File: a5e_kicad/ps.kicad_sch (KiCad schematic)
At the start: 52 parts, among them U1302 SIC931BED-T1-GE3

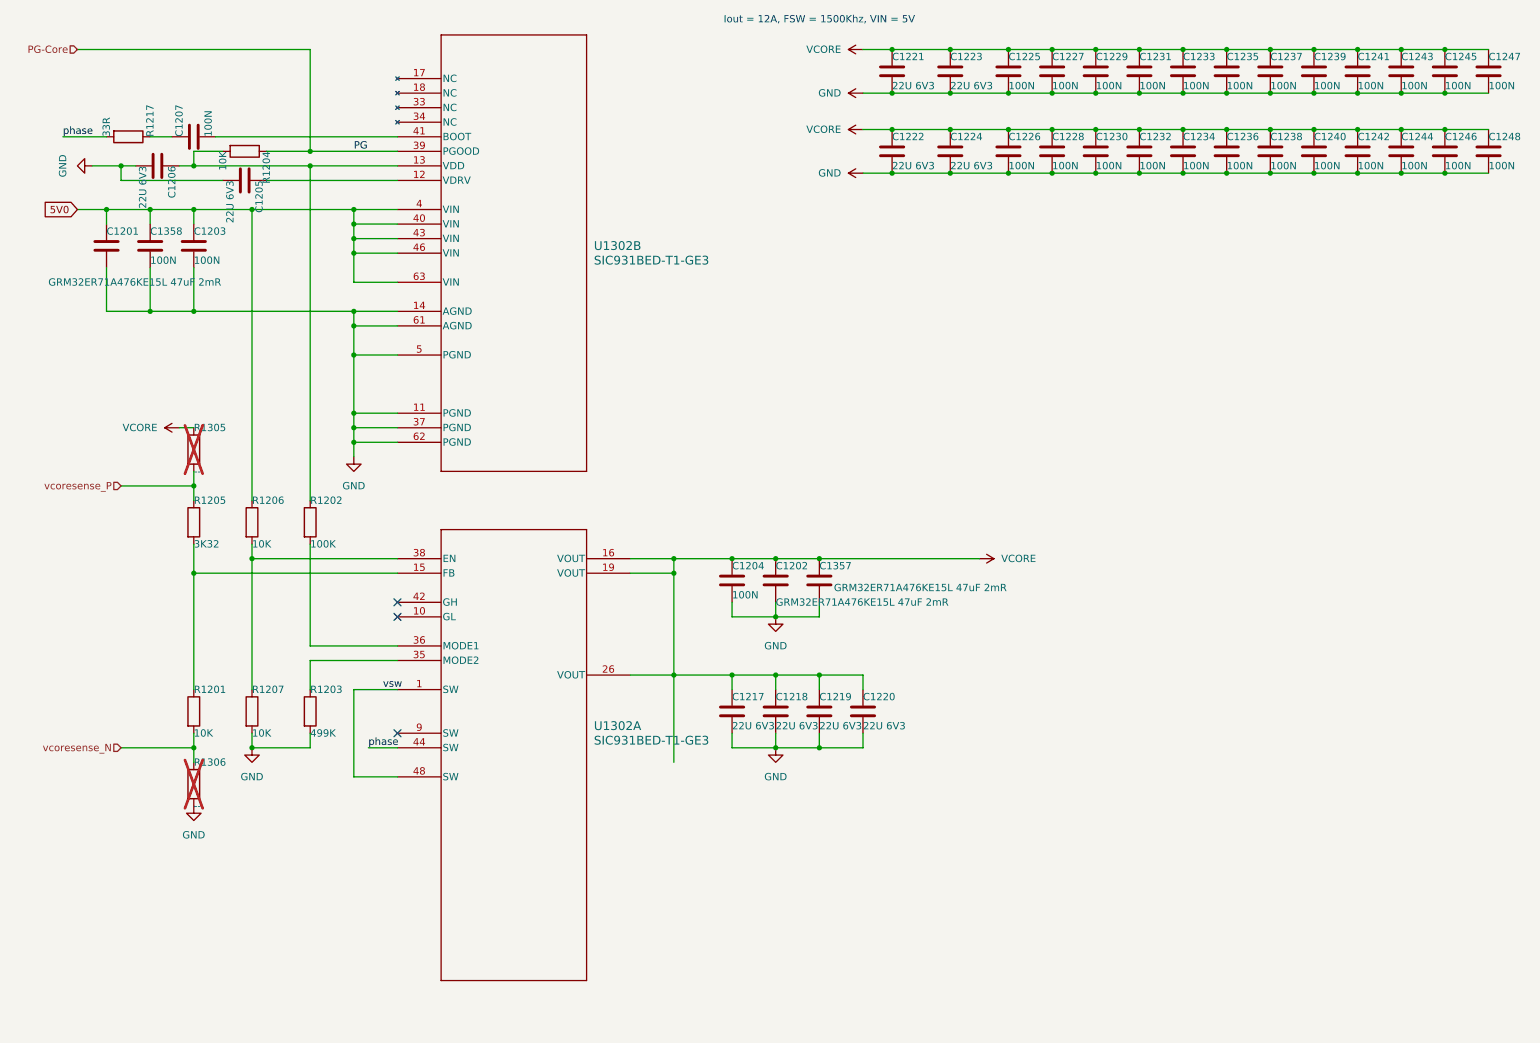
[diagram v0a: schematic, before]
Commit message: add vias to lppdr balls
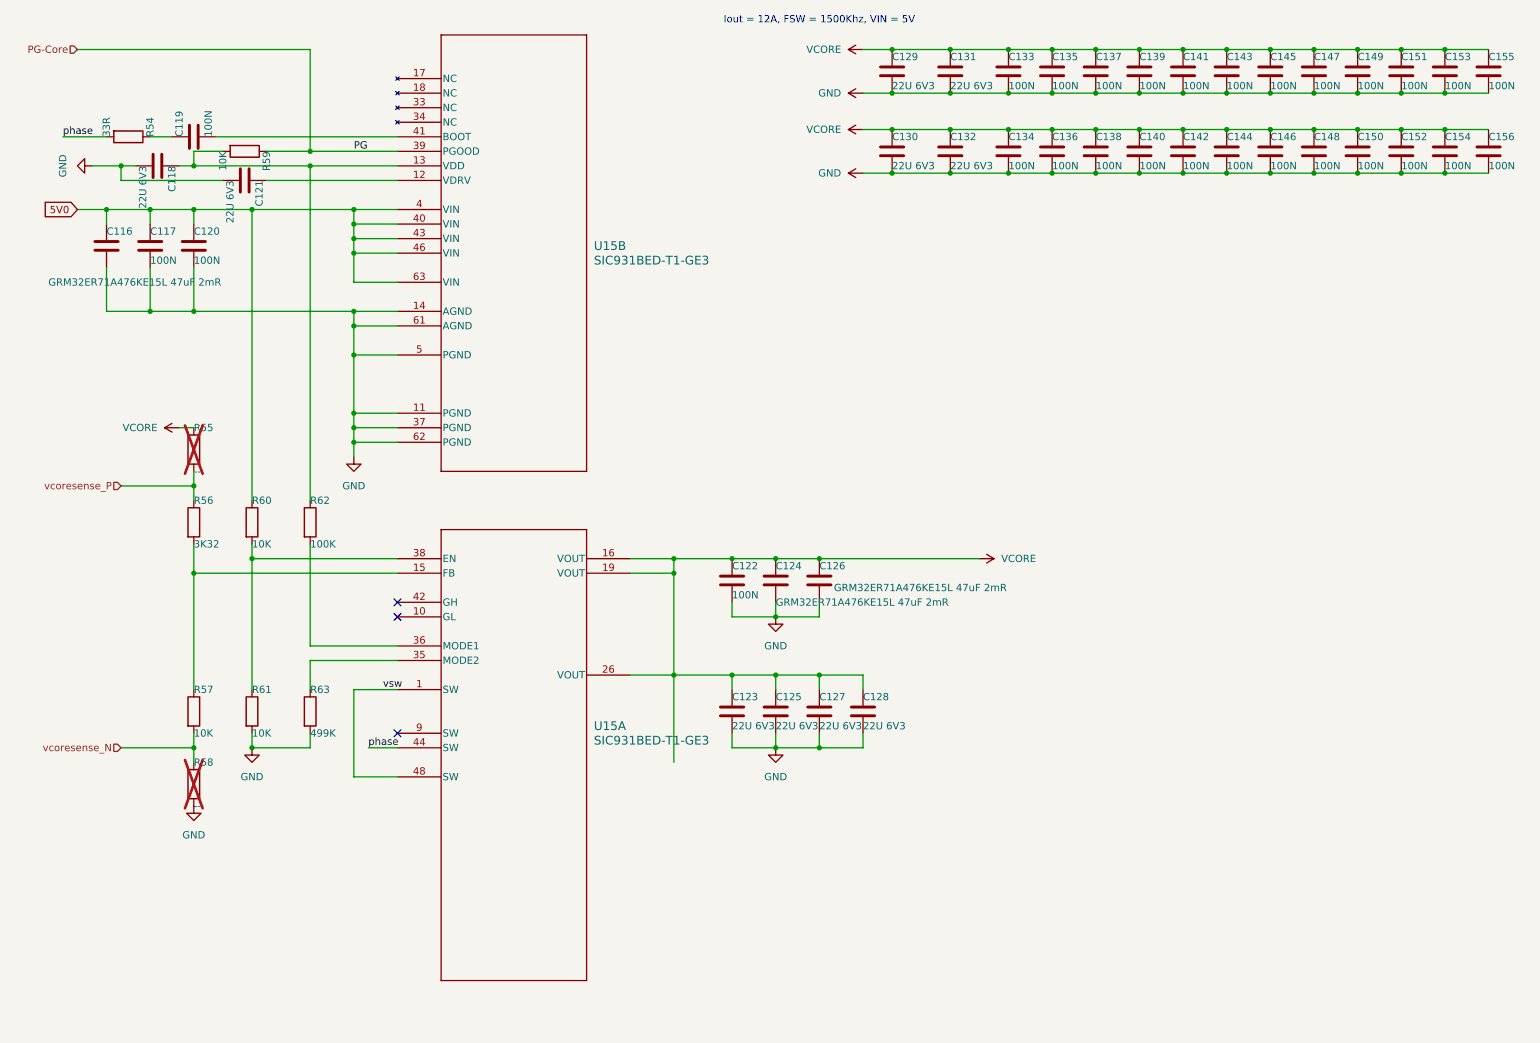
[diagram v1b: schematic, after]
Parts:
- renumbered C1201 to C116, C1358 to C117, C1206 to C118, C1207 to C119, C1203 to C120, C1205 to C121, C1204 to C122, C1217 to C123, C1202 to C124, C1218 to C125, C1357 to C126, C1219 to C127, C1220 to C128, C1221 to C129, C1222 to C130, C1223 to C131, C1224 to C132, C1225 to C133, C1226 to C134, C1227 to C135, C1228 to C136, C1229 to C137, C1230 to C138, C1231 to C139, C1232 to C140, C1233 to C141, C1234 to C142, C1235 to C143, C1236 to C144, C1237 to C145, C1238 to C146, C1239 to C147, C1240 to C148, C1241 to C149, C1242 to C150, C1243 to C151, C1244 to C152, C1245 to C153, C1246 to C154, C1247 to C155, C1248 to C156, R1217 to R54, R1305 to R55, R1205 to R56, R1201 to R57, R1306 to R58, R1204 to R59, R1206 to R60, R1207 to R61, R1202 to R62, R1203 to R63, U1302 to U15

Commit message: add comments
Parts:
- removed R55, R58: --, Resistor_SMD:R_0402_1005Metric, symbol Device:R
- removed R56: 3K32, Resistor_SMD:R_0402_1005Metric, symbol Device:R
- removed R57, R60, R61: 10K, Resistor_SMD:R_0402_1005Metric, symbol Device:R
- removed R62: 100K, Resistor_SMD:R_0402_1005Metric, symbol Device:R
- removed R63: 499K, Resistor_SMD:R_0402_1005Metric, symbol Device:R
- removed U15: SIC931BED-T1-GE3, symbol SiC931bed:SIC931BED-T1-GE3
- added L1: 250n, agilex_lib:CMLE051H, symbol Device:L
- added U15: (no value), agilex_lib:TDA38812, symbol agilex_5_lib:TDA38812
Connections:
- net 5V0: now also U15.19 (VCC)
- net VCORE: now also L1.2
- net vcoresense_N: now also U15.7 (FB)
- net vcoresense_P: now also U15.6 (RGND)
- new net: L1.1, U15.20 (SW)
- no-connect marks 3 -> 0
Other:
- moved on the sheet: C122, C123, C124, C125, C126, C127, C128

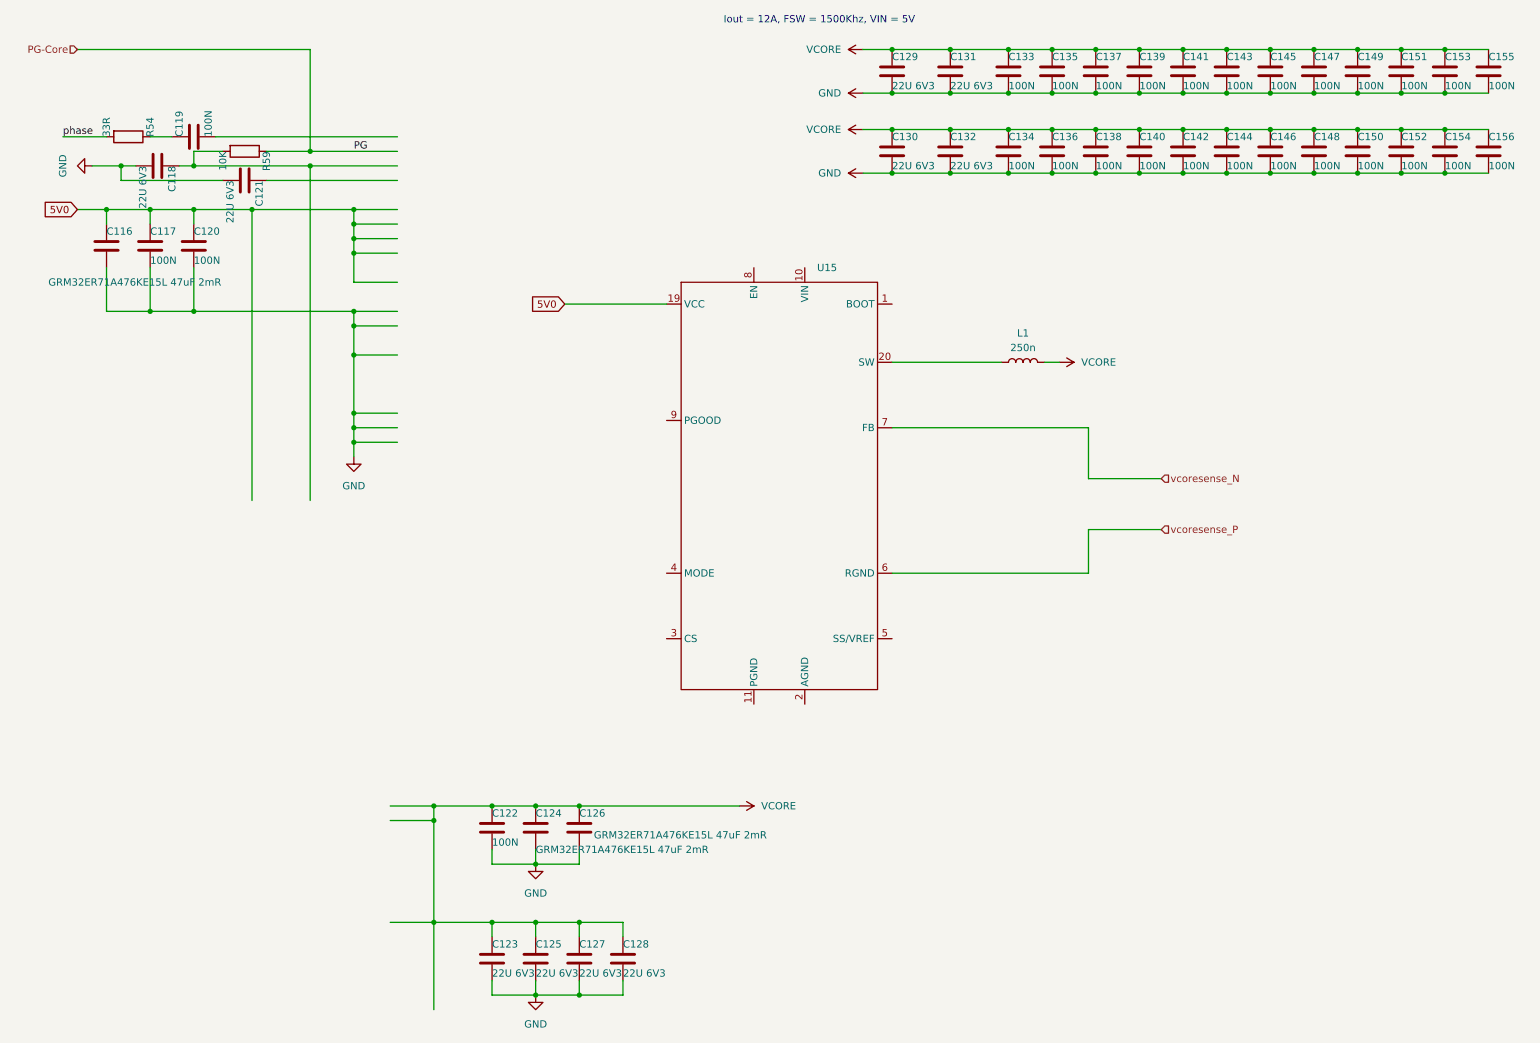
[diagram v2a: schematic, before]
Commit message: start routing power supplies
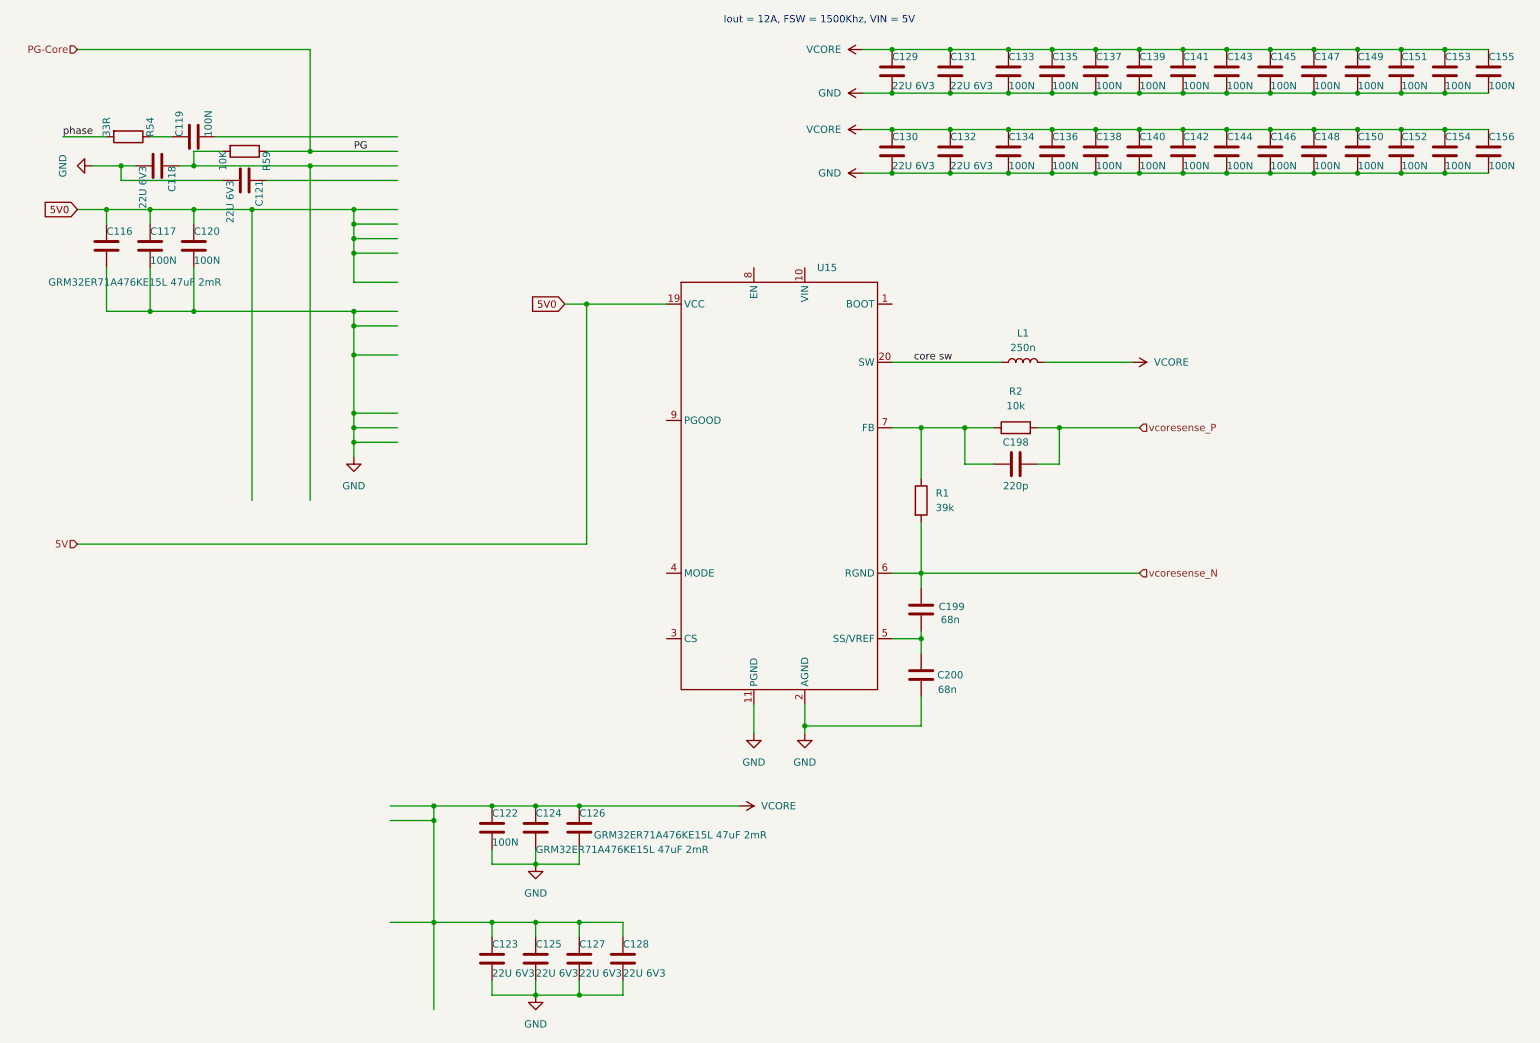
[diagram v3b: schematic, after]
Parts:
- added C198: 220p, Capacitor_SMD:C_0402_1005Metric, symbol Device:C
- added C199, C200: 68n, Capacitor_SMD:C_0402_1005Metric, symbol Device:C
- added R1: 39k, Resistor_SMD:R_0402_1005Metric, symbol Device:R
- added R2: 10k, Resistor_SMD:R_0402_1005Metric, symbol Device:R
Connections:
- net GND: now also U15.11 (PGND), U15.2 (AGND), C200.1
- net vcoresense_N: now also U15.6 (RGND), C199.2, R1.2; no longer U15.7 (FB)
- net vcoresense_P: now also C198.2, R2.2; no longer U15.6 (RGND)
- net core sw: now reaches L1.1, U15.20 (SW)
- net at U15.5 (SS/VREF): now also C199.1, C200.2
- new net: C198.1, R1.1, R2.1, U15.7 (FB)

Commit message: add capacitors and resistors to core power
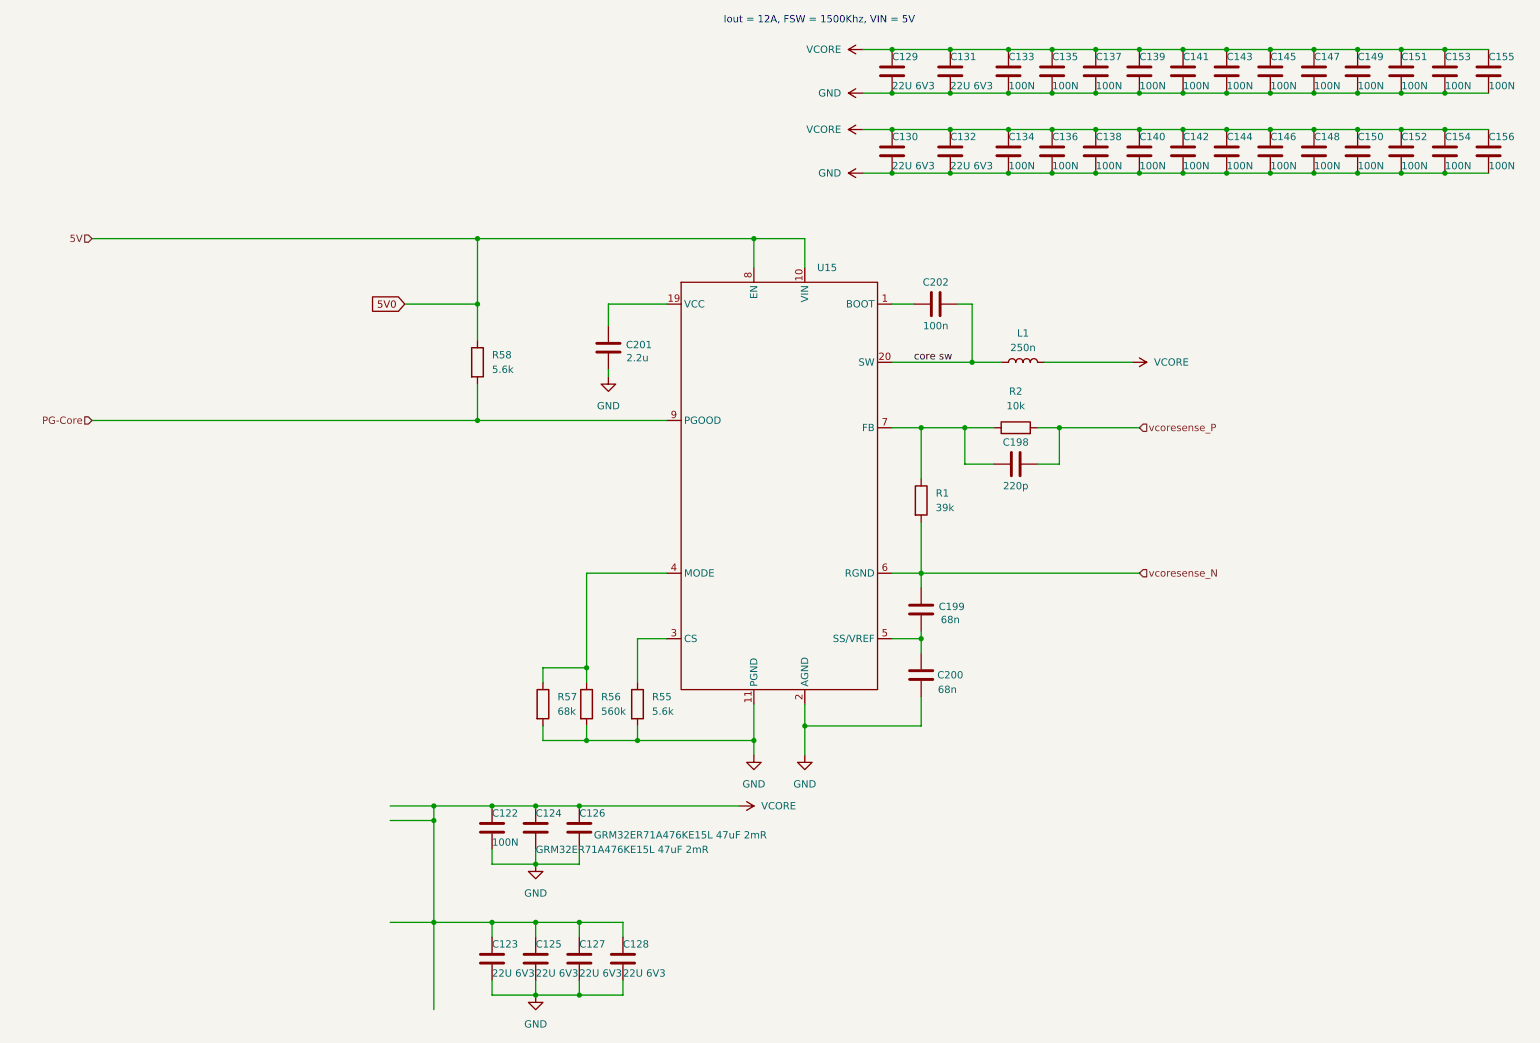
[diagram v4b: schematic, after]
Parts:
- removed C116: GRM32ER71A476KE15L 47uF 2mR, Capacitor_SMD:C_1210_3225Metric, symbol Device:C
- removed C117, C119, C120: 100N, Capacitor_SMD:C_0402_1005Metric, symbol Device:C
- removed C118, C121: 22U 6V3, Capacitor_SMD:C_0402_1005Metric, symbol Device:C
- removed R54: 33R, Resistor_SMD:R_0402_1005Metric, symbol Device:R
- removed R59: 10K, Resistor_SMD:R_0402_1005Metric, symbol Device:R
- added C201: 2.2u, Capacitor_SMD:C_0402_1005Metric, symbol Device:C
- added C202: 100n, Capacitor_SMD:C_0402_1005Metric, symbol Device:C
- added R55, R58: 5.6k, Resistor_SMD:R_0402_1005Metric, symbol Device:R
- added R56: 560k, Resistor_SMD:R_0402_1005Metric, symbol Device:R
- added R57: 68k, Resistor_SMD:R_0402_1005Metric, symbol Device:R
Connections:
- net 5V0: now also U15.10 (VIN), U15.8 (EN), R58.1; no longer U15.19 (VCC)
- net GND: now also C201.1, R55.2, R56.2, R57.2
- net PG-Core: now also U15.9 (PGOOD), R58.2
- net core sw: now also C202.2
- net at U15.1 (BOOT): now also C202.1
- net at U15.3 (CS): now also R55.1
- net at U15.4 (MODE): now also R56.1, R57.1
- new net: C201.2, U15.19 (VCC)

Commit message: sketch length matching for lpddr4
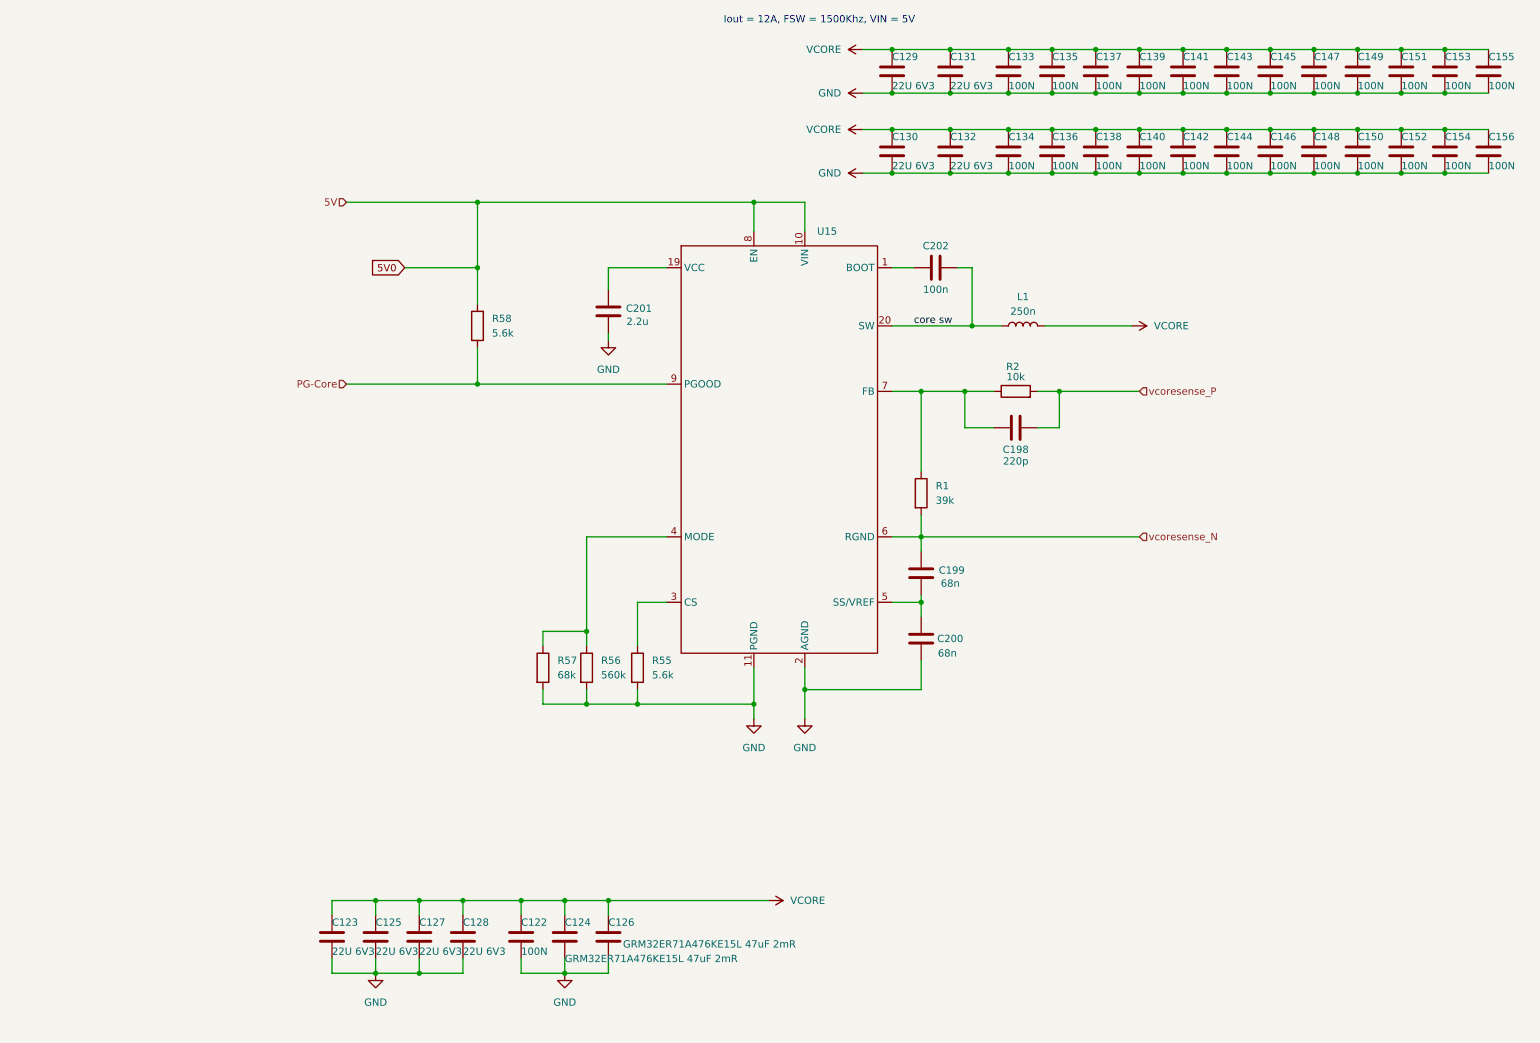
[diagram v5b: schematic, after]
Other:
- moved on the sheet: C122, C123, C124, C125, C126, C127, C128, C198, C199, C200, C201, C202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
